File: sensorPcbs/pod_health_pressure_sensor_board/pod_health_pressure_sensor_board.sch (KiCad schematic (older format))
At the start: 2 parts, among them J1 RJ45, U1 bmp180

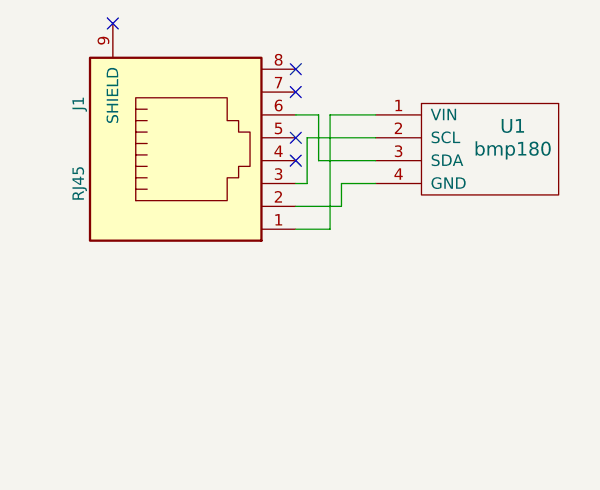
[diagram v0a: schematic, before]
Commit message: changed all the sensor PCB schematics and added the global component schematic library into each project
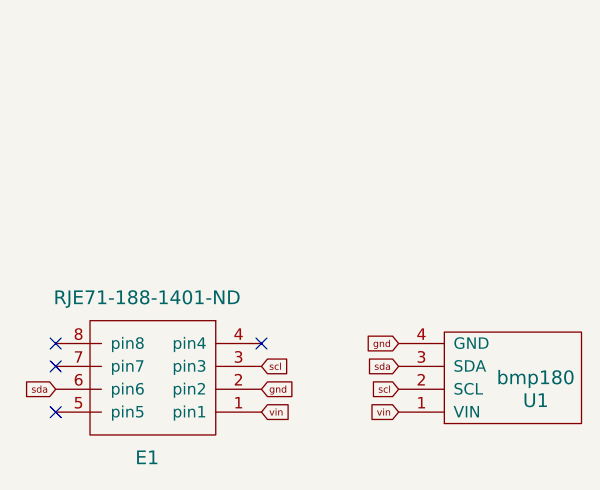
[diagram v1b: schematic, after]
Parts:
- removed J1: RJ45, Connectors:RJ45_8, symbol RJ45
- added E1: RJE71-188-1401-ND, symbol RJE71-188-1401-ND
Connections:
- net vin: now reaches U1.1 (VIN)
- net vin: now also E1.1 (pin1)
- net gnd: now reaches U1.4 (GND)
- net gnd: now also E1.2 (pin2)
- net scl: now reaches U1.2 (SCL)
- net scl: now also E1.3 (pin3)
- net sda: now reaches U1.3 (SDA)
- net sda: now also E1.6 (pin6)
- no-connect marks 5 -> 4
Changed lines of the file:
@@
 EESchema Schematic File Version 2
-LIBS:power
-LIBS:device
-LIBS:transistors
-LIBS:conn
-LIBS:linear
-LIBS:regul
-LIBS:74xx
-LIBS:cmos4000
-LIBS:adc-dac
-LIBS:memory
-LIBS:xilinx
-LIBS:microcontrollers
-LIBS:dsp
-LIBS:microchip
-LIBS:analog_switches
-LIBS:motorola
-LIBS:texas
-LIBS:intel
-LIBS:audio
-LIBS:interface
-LIBS:digital-audio
-LIBS:philips
-LIBS:display
-LIBS:cypress
-LIBS:siliconi
-LIBS:opto
-LIBS:atmel
-LIBS:contrib
-LIBS:valves
 LIBS:bmp180
+LIBS:customSchematics
 LIBS:pod_health_pressure_sensor_board-cache
 EELAYER 25 0
@@
 $EndDescr
 $Comp
-L RJ45 J1
-U 1 1 58D71404
-P 2200 2150
-F 0 "J1" H 2400 2650 50  0000 C CNN
-F 1 "RJ45" H 2050 2650 50  0000 C CNN
-F 2 "Connectors:RJ45_8" H 2200 2150 50  0001 C CNN
-F 3 "" H 2200 2150 50  0001 C CNN
-	1    2200 2150
-	0    -1   -1   0
+L RJE71-188-1401-ND E1
+U 1 1 59711E0A
+P 2300 3300
+F 0 "E1" H 2600 3500 60  0000 C CNN
+F 1 "RJE71-188-1401-ND" H 2600 2800 60  0000 C CNN
+F 2 "" H 2300 3300 60  0001 C CNN
+F 3 "" H 2300 3300 60  0001 C CNN
+	1    2300 3300
+	-1   0    0    1
 $EndComp
-NoConn ~ 1850 1600
-NoConn ~ 2650 1800
-NoConn ~ 2650 1900
 $Comp
 L bmp180 U1
-U 1 1 58ED5750
-P 3000 2450
-F 0 "U1" H 3600 2850 60  0000 C CNN
-F 1 "bmp180" H 3600 2750 60  0000 C CNN
-F 2 "bmp180_footprints:bmp180" H 3000 2450 60  0001 C CNN
-F 3 "" H 3000 2450 60  0001 C CNN
-	1    3000 2450
-	1    0    0    -1
+U 1 1 59711E9E
+P 3100 2850
+F 0 "U1" H 3700 3250 60  0000 C CNN
+F 1 "bmp180" H 3700 3150 60  0000 C CNN
+F 2 "bmp180_footprints:bmp180" H 3100 2850 60  0001 C CNN
+F 3 "" H 3100 2850 60  0001 C CNN
+	1    3100 2850
+	1    0    0    1
 $EndComp
-Wire Wire Line
-	3000 2000 2800 2000
-Wire Wire Line
-	2800 2000 2800 2500
-Wire Wire Line
-	2800 2500 2650 2500
-Wire Wire Line
-	3000 2300 2850 2300
-Wire Wire Line
-	2850 2300 2850 2400
-Wire Wire Line
-	2850 2400 2650 2400
-Wire Wire Line
-	3000 2100 2700 2100
-Wire Wire Line
-	2700 2100 2700 2300
-Wire Wire Line
-	2700 2300 2650 2300
-Wire Wire Line
-	3000 2200 2750 2200
-Wire Wire Line
-	2750 2200 2750 2000
-Wire Wire Line
-	2750 2000 2650 2000
-NoConn ~ 2650 2100
-NoConn ~ 2650 2200
+Text GLabel 3100 3300 0    30   Input ~ 0
+vin
+Text GLabel 3100 3200 0    30   Input ~ 0
+scl
+Text GLabel 3100 3100 0    30   Input ~ 0
+sda
+Text GLabel 3100 3000 0    30   Input ~ 0
+gnd
+Text GLabel 2500 3300 2    30   Input ~ 0
+vin
+Text GLabel 2500 3100 2    30   Input ~ 0
+scl
+Text GLabel 1600 3200 0    30   Input ~ 0
+sda
+Text GLabel 2500 3200 2    30   Input ~ 0
+gnd
+NoConn ~ 2500 3000
+NoConn ~ 1600 3000
+NoConn ~ 1600 3100
+NoConn ~ 1600 3300
 $EndSCHEMATC

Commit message: added all the ferkin new ethernet shields to the sensor pcbs
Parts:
- E1: footprint (none) -> footprints:RJE71-188-1401-ND
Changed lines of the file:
@@
 F 0 "E1" H 2600 3500 60  0000 C CNN
 F 1 "RJE71-188-1401-ND" H 2600 2800 60  0000 C CNN
-F 2 "" H 2300 3300 60  0001 C CNN
+F 2 "footprints:RJE71-188-1401-ND" H 2300 3300 60  0001 C CNN
 F 3 "" H 2300 3300 60  0001 C CNN
 	1    2300 3300
